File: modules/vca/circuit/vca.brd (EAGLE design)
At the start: 100 x 80 mm, 51 parts, among them IC1 LM324N, IC2 LM324N

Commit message: VCA design
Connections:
- net +12V: now also R25.P$1
- net +5V: no longer R25.P$1
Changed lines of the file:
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@@
 <contactref element="R18" pad="P$2"/>
 <contactref element="R22" pad="P$2"/>
-<contactref element="R25" pad="P$1"/>
 <wire x1="48.26" y1="55.88" x2="58.42" y2="59.69" width="0" layer="19" extent="1-1"/>
 <wire x1="38.1" y1="52.07" x2="48.26" y2="55.88" width="0" layer="19" extent="1-1"/>
-<wire x1="30.48" y1="63.5" x2="38.1" y2="52.07" width="0" layer="19" extent="1-1"/>
-<wire x1="17.78" y1="59.69" x2="30.48" y2="63.5" width="0" layer="19" extent="1-1"/>
 <wire x1="49.53" y1="35.56" x2="38.1" y2="52.07" width="0" layer="19" extent="1-1"/>
+<wire x1="17.78" y1="59.69" x2="38.1" y2="52.07" width="0" layer="19" extent="1-1"/>
 </signal>
 <signal name="+12V">
@@
 <contactref element="C5" pad="2"/>
 <contactref element="IC1" pad="4"/>
-<wire x1="49.53" y1="15.24" x2="29.21" y2="15.24" width="0" layer="19" extent="1-1"/>
-<wire x1="39.37" y1="33.02" x2="29.21" y2="15.24" width="0" layer="19" extent="1-1"/>
+<contactref element="R25" pad="P$1"/>
+<wire x1="11.557" y1="67.31" x2="30.48" y2="63.5" width="0" layer="19" extent="1-1"/>
+<wire x1="39.37" y1="33.02" x2="30.48" y2="63.5" width="0" layer="19" extent="1-1"/>
 <wire x1="52.07" y1="35.56" x2="39.37" y2="33.02" width="0" layer="19" extent="1-1"/>
-<wire x1="11.557" y1="67.31" x2="39.37" y2="33.02" width="0" layer="19" extent="1-1"/>
+<wire x1="49.53" y1="15.24" x2="39.37" y2="33.02" width="0" layer="19" extent="1-1"/>
+<wire x1="29.21" y1="15.24" x2="49.53" y2="15.24" width="0" layer="19" extent="1-1"/>
 </signal>
 <signal name="-12V">

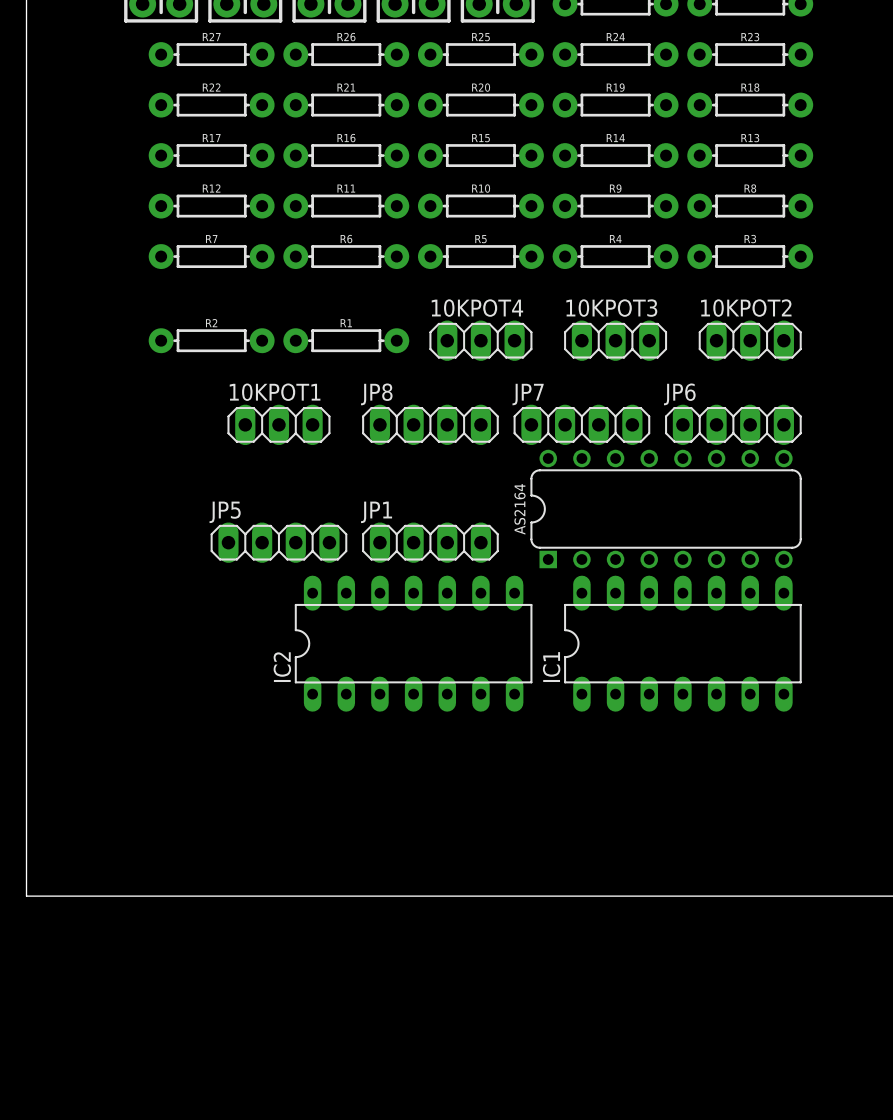
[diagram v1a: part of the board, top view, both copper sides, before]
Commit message: Resistor changes for vca
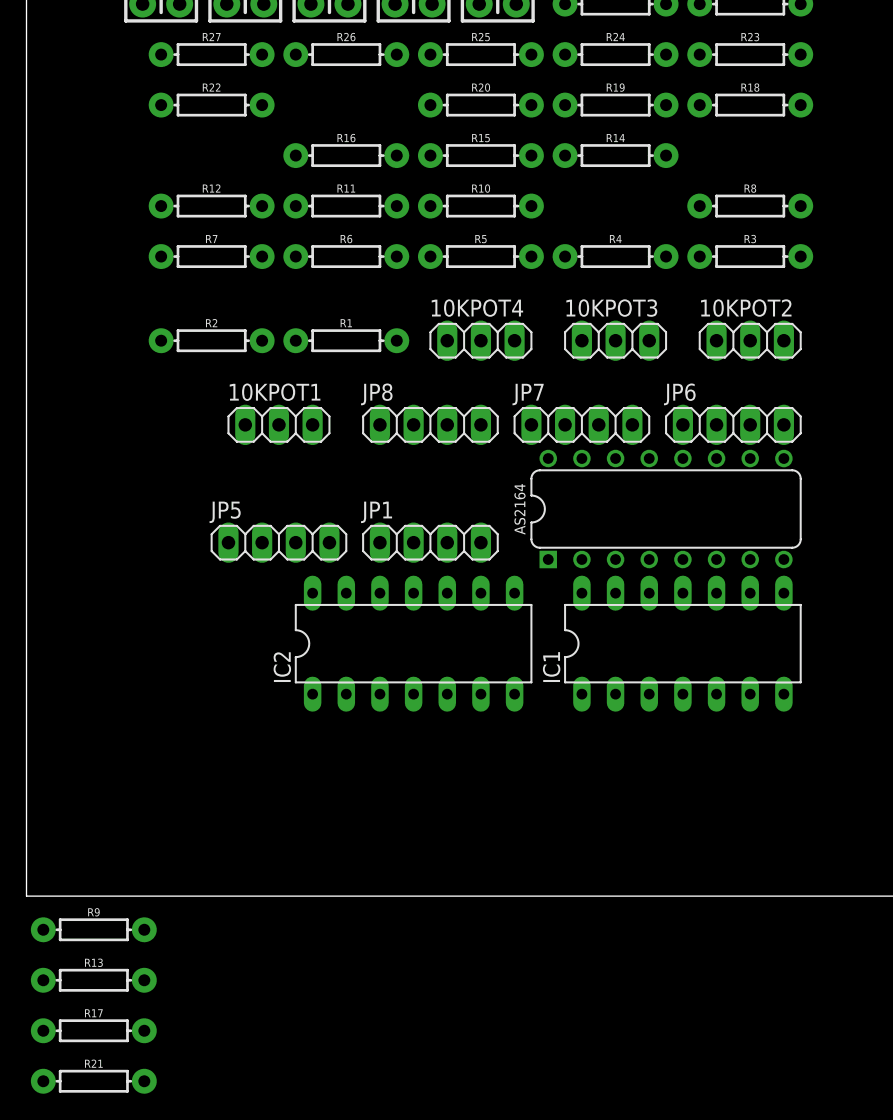
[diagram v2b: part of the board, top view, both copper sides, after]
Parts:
- R10, R14, R18, R22: value 1.5k -> 16.5k
- R11, R15, R19, R23: value 5k -> 50k
- R12, R16, R20, R24: value 3.3k -> 33k
- moved R13 79.5 mm to (5.08, -6.35)
- moved R21 76.1 mm to (5.08, -14.0)
- moved R9 67.3 mm to (5.08, -2.54)
- moved R17 66.6 mm to (5.08, -10.2)
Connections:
- net GND: now also R13.P$2, R17.P$2, R21.P$2, R9.P$2; no longer R13.P$1, R17.P$1, R21.P$1, R9.P$1
- net IN_CV1: now also R9.P$1
- net IN_CV2: now also R13.P$1
- net IN_CV3: now also R17.P$1
- net IN_CV4: now also R21.P$1
- net N$10: no longer R9.P$2
- net N$13: no longer R13.P$2
- net N$16: no longer R17.P$2
- net N$19: no longer R21.P$2

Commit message: vca changes
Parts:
- removed 10KPOT1, 10KPOT2, 10KPOT3, 10KPOT4: (no value), pinhead:1X03
- R11, R15, R19, R23: value 50k -> 47k
- R12, R16, R20, R24: value 33k -> 30k
- R13, R17, R21: value 1k -> 16.5k
- R14, R18, R22: value 16.5k -> 10k
- R9: value 1k -> 10k
- moved R18 108.5 mm to (5.08, -36.8)
- moved R22 104.5 mm to (5.08, -44.5)
- moved R14 93.8 mm to (5.08, -29.2)
- moved R10 75.7 mm to (5.08, -17.8)
- moved R21 26.7 mm to (5.08, -40.6)
- moved R17 22.9 mm to (5.08, -33.0)
- moved R9 19.1 mm to (5.08, -21.6)
- moved R13 19.0 mm to (5.08, -25.4)
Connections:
- removed net N$15: 10KPOT1.2, IC2.3
- removed net N$16: 10KPOT1.1, R18.P$1
- removed net N$18: 10KPOT4.2, IC2.12
- removed net N$19: 10KPOT4.1, R22.P$1
- net +5V: now also R10.P$1, R13.P$1, R17.P$1, R21.P$1; no longer R10.P$2, R14.P$2, R18.P$2, R22.P$2
- net GND: now also IC1.10, IC1.12, IC1.3, IC1.5, R14.P$1, R18.P$1, R22.P$1, R9.P$1; no longer 10KPOT1.3, 10KPOT2.3, 10KPOT3.3, 10KPOT4.3, IC1.13, IC1.2, IC1.6, IC1.9, R13.P$2, R17.P$2, R21.P$2, R9.P$2
- net IN_CV1: no longer R9.P$1
- net IN_CV2: no longer R13.P$1
- net IN_CV3: no longer R17.P$1
- net IN_CV4: no longer R21.P$1
- net N$10: now also IC2.3, R10.P$2, R9.P$2; no longer 10KPOT3.1, R10.P$1
- net N$12: now also IC2.10, R17.P$2, R18.P$2; no longer 10KPOT2.2, IC2.5
- net N$13: now also IC2.12, R21.P$2, R22.P$2; no longer 10KPOT2.1, R14.P$1
- net N$25: now also IC1.13; no longer IC1.12
- net N$31: now also IC1.9; no longer IC1.10
- net N$32: now also IC1.6; no longer IC1.5
- net N$33: now also IC1.2; no longer IC1.3
- net N$9: now also IC2.5, R13.P$2, R14.P$2; no longer 10KPOT3.2, IC2.10

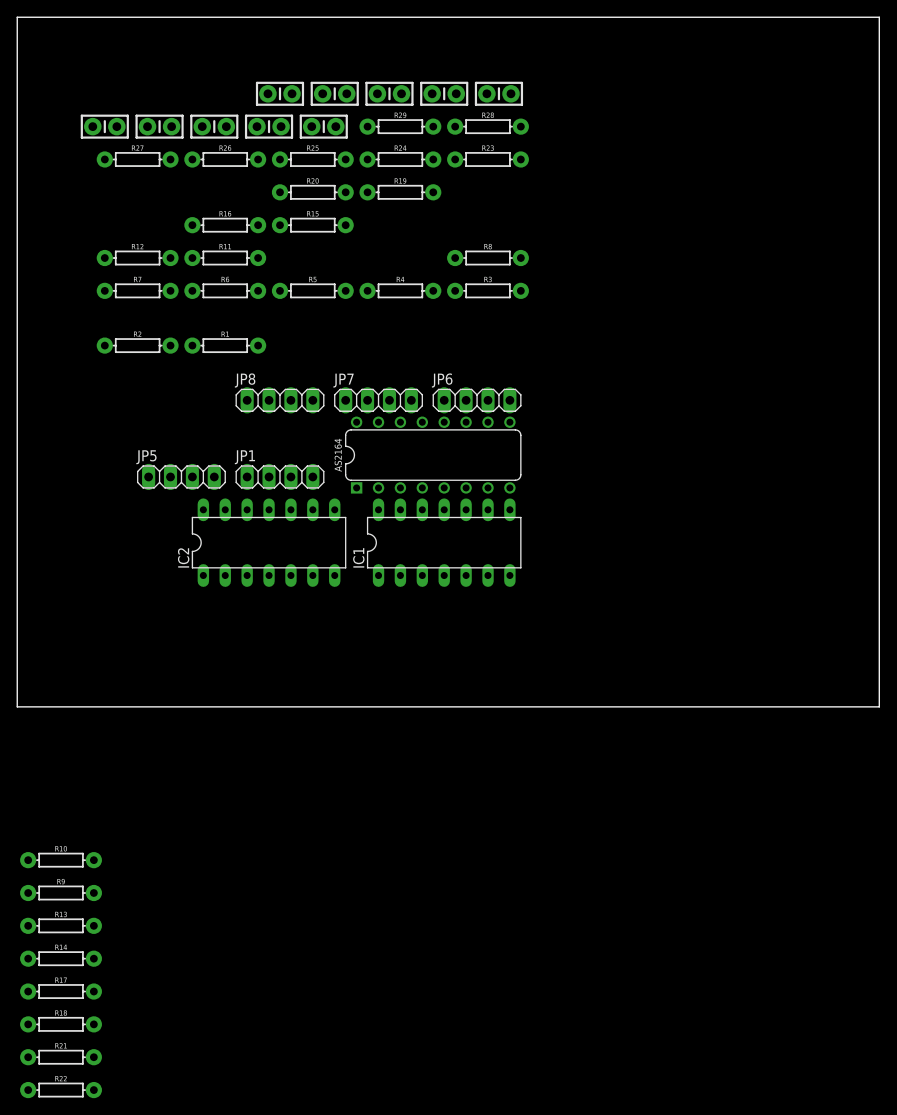
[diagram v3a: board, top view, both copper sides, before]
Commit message: modified VCA
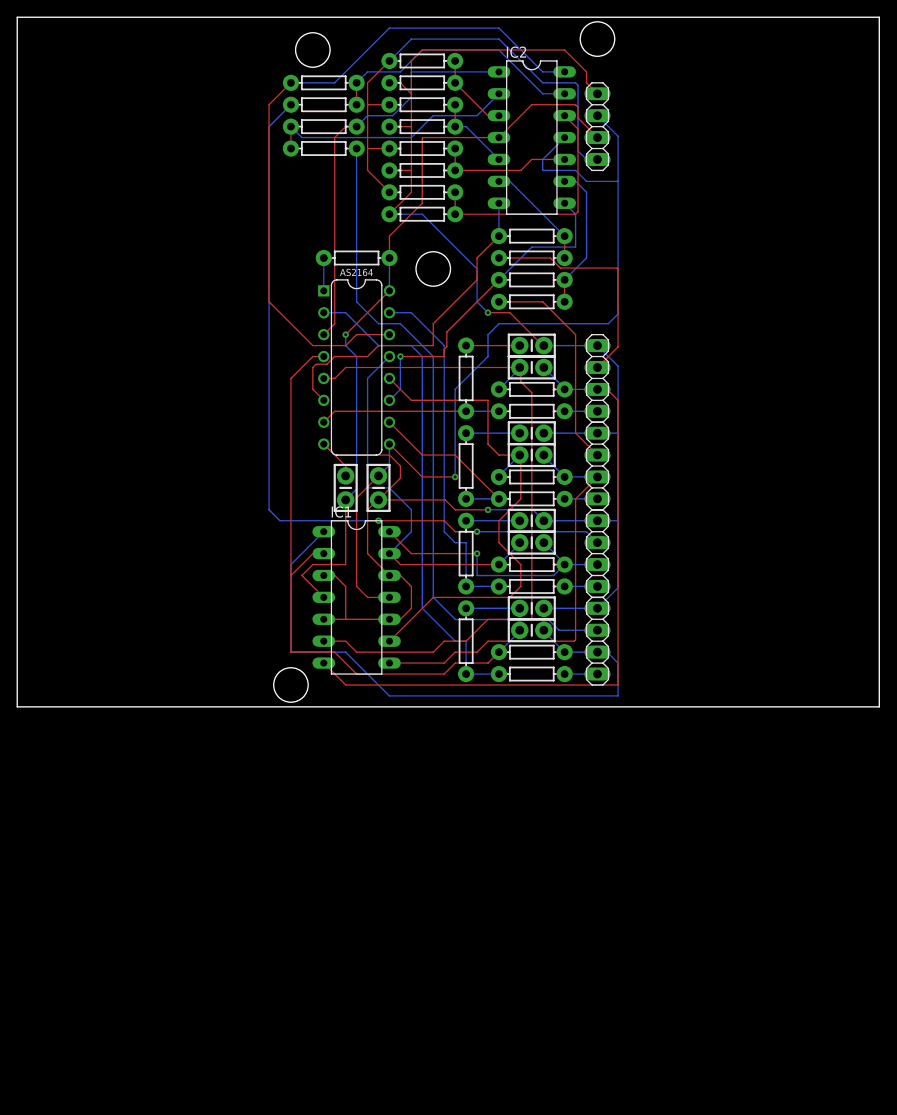
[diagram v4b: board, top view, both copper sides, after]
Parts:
- R10, R13, R17, R21: value 16.5k -> 1k
- R11, R15, R19, R23: value 47k -> 100k
- R12, R16, R20, R24: value 30k -> 50k
- R14, R18, R22, R9: value 10k -> 500
- moved R22 109.9 mm to (47.0, 57.1)
- moved R21 108.7 mm to (47.0, 59.7)
- moved R18 107.6 mm to (47.0, 62.2)
- moved R17 106.4 mm to (47.0, 64.8)
- moved R14 105.2 mm to (47.0, 67.3)
- moved R13 104.1 mm to (47.0, 69.8)
- moved R9 102.9 mm to (47.0, 72.4)
- moved R10 101.7 mm to (47.0, 74.9)
- moved C10 68.7 mm to (59.7, 8.89)
- moved C4 62.9 mm to (59.7, 21.6), turned to 180 degrees
- moved R29 62.8 mm to (59.7, 6.35)
- moved C1 60.9 mm to (59.7, 11.4), turned to 180 degrees
- moved R26 58.9 mm to (59.7, 16.5)
- moved R27 58.7 mm to (59.7, 26.7)
- moved IC2 56.0 mm to (59.7, 66.0), turned to 270 degrees
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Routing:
- net GND: track 0.00 -> 213.9 mm, vias 0 -> 2
- net -12V: track 0.00 -> 103.9 mm, vias 0 -> 1
- net IN_CV4: track 0.00 -> 87.7 mm, vias 0 -> 2
- net +12V: track 0.00 -> 87.7 mm, vias 0 -> 1
- net N$32: track 0.00 -> 82.9 mm
- net CV4: track 0.00 -> 79.5 mm
- net OUT2: track 0.00 -> 78.5 mm
- net IN_CV1: track 0.00 -> 77.9 mm
- net N$33: track 0.00 -> 71.2 mm
- net OUT1: track 0.00 -> 69.7 mm
- net N$31: track 0.00 -> 60.6 mm
- net +5V: track 0.00 -> 57.9 mm
- net N$1: track 0.00 -> 57.0 mm
- net OUT3: track 0.00 -> 50.0 mm
- net CV1: track 0.00 -> 47.3 mm
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
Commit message: Finished VCA
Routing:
- net IN_CV4: track 87.7 -> 84.0 mm
- net OUT1: track 69.7 -> 71.9 mm
- net N$33: track 71.2 -> 70.2 mm
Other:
- board size 100 x 80 mm -> 47.9 x 80 mm
- board text added: "+12"
- board text added: "+5"
- board text added: "-12"
- board text added: "0.1uf"
- board text added: "100pf"
- board text added: "560pf"
- board text added: "CV"
- board text added: "DUMAIS"
- board text added: "G"
- board text added: "IN"
- board text added: "O"
- board text added: "Quad VCA"
